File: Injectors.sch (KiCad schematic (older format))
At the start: 36 parts, among them Q1 VND14NV04, Q2 VND14NV04, Q3 VND14NV04, Q4 VND14NV04, Q5 VND14NV04, Q6 VND14NV04

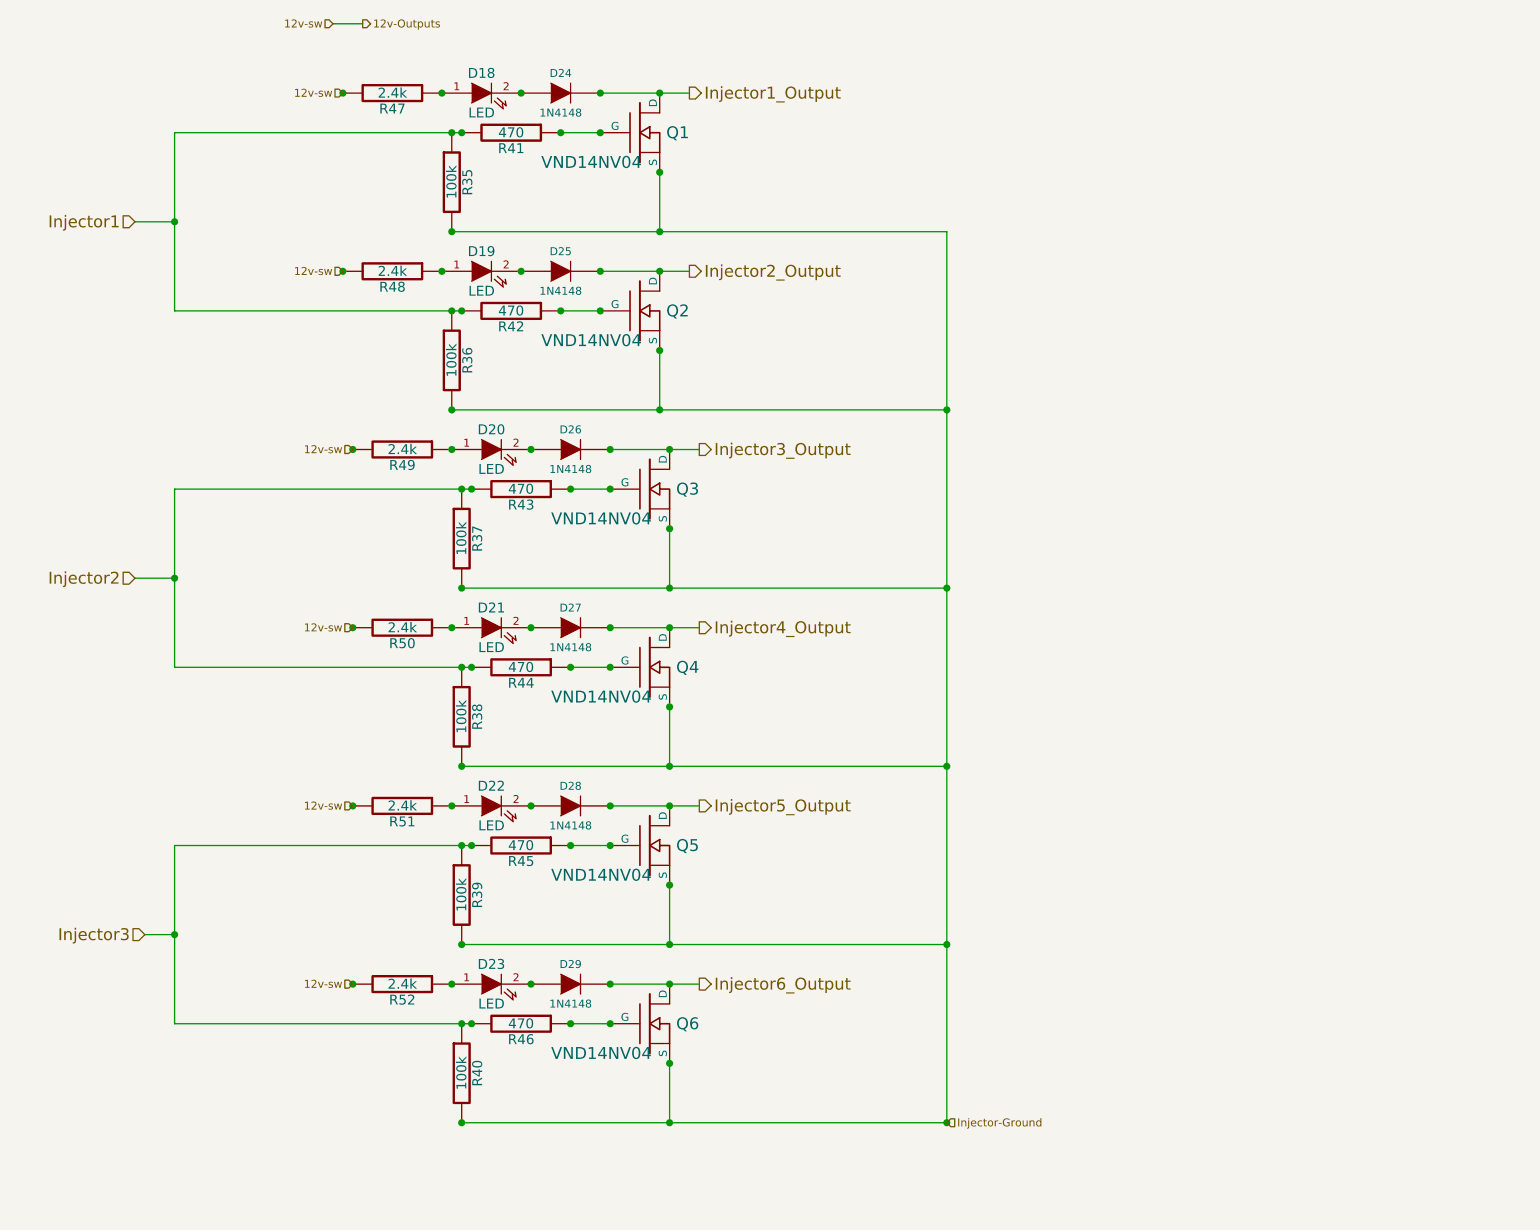
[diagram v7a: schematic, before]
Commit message: Schematics, PDF, BOM updated with latest changes
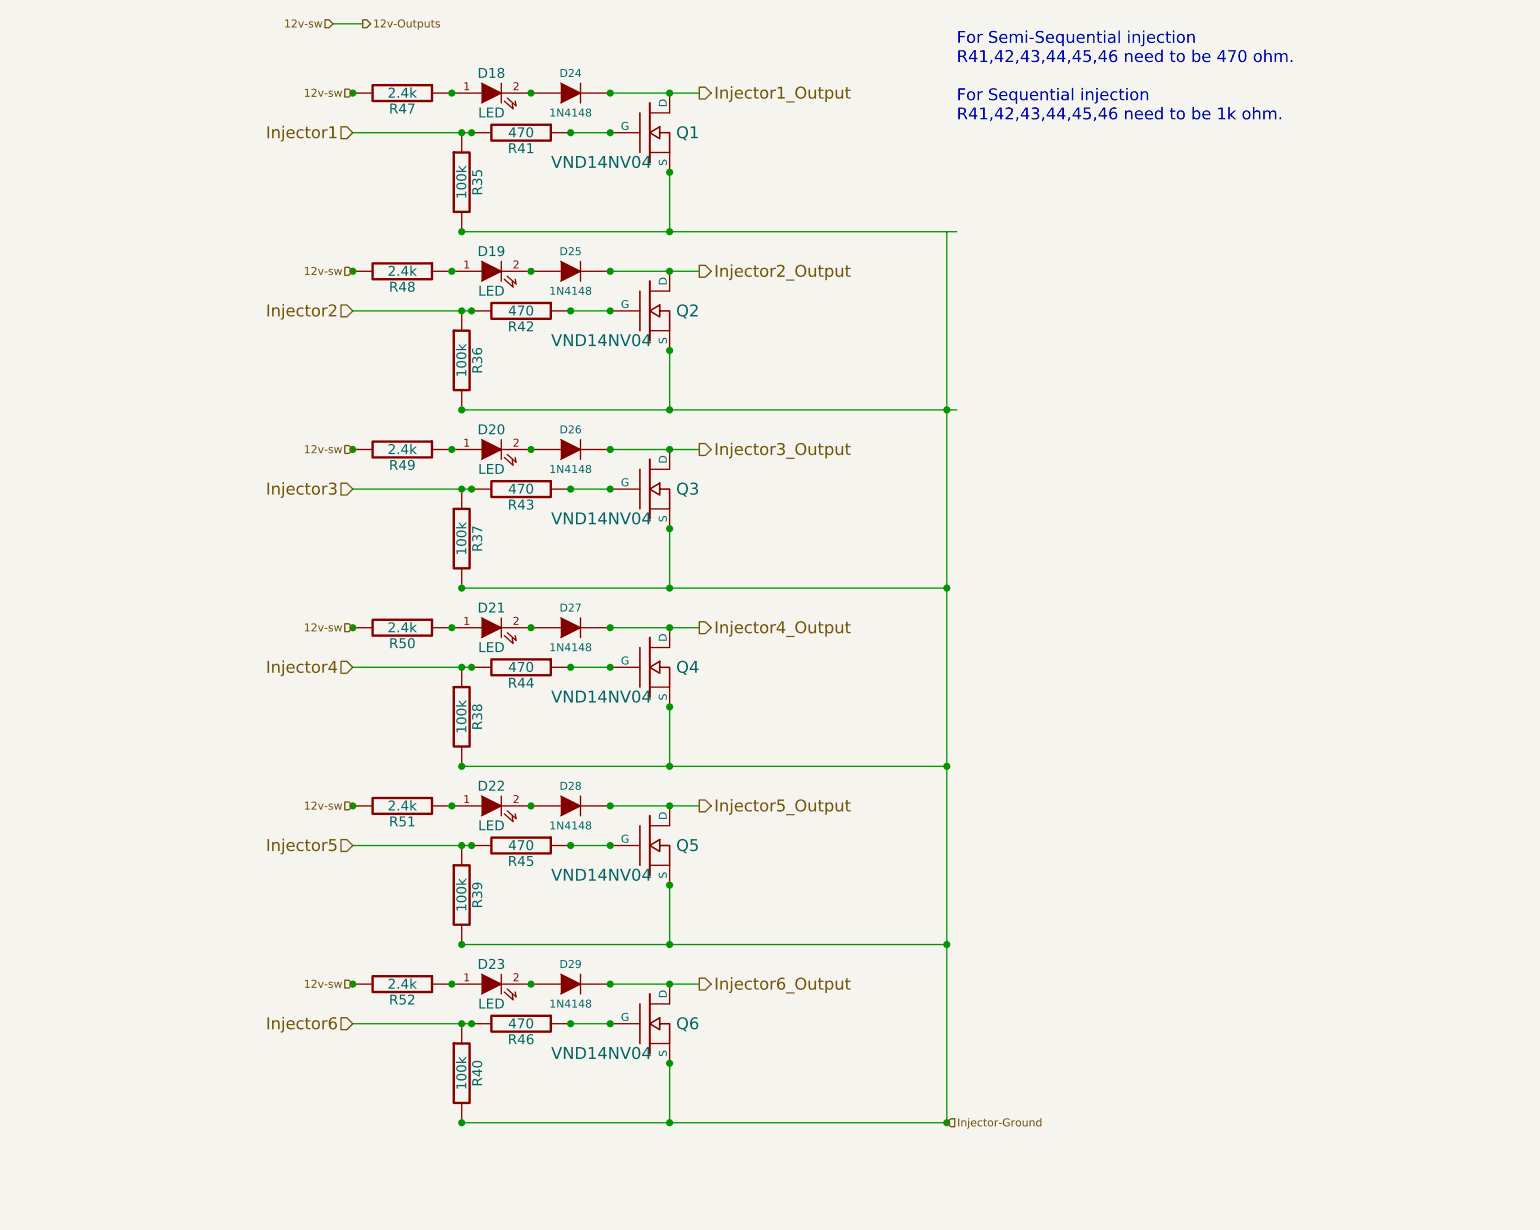
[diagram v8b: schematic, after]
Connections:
- net labels added: Injector4, Injector5, Injector6
- wire segments 38 -> 32
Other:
- note added: "For Semi-Sequential injection\nR41,42,43,44,45,46 need to be 470 ohm.\n\nFor Sequential injection \nR41,42,43,44,45,46 need to be 1k ohm."
- moved on the sheet: D18, D19, D24, D25, Q1, Q2, R35, R36, R41, R42, R47, R48
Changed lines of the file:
@@
-EESchema Schematic File Version 2  date Mon 23 Jan 2012 10:59:50 PM EST
+EESchema Schematic File Version 2  date Tue 24 Jan 2012 02:18:15 PM EST
 LIBS:power
 LIBS:device
@@
 EELAYER END
 $Descr A4 11700 8267
-Sheet 4 7
+Sheet 6 7
 Title "Jaguar PCB for FreeEMS"
 Date "24 jan 2012"
@@
 Comment4 ""
 $EndDescr
+Text Notes 5450 1400 0    60   ~ 0
+For Semi-Sequential injection\nR41,42,43,44,45,46 need to be 470 ohm.\n\nFor Sequential injection \nR41,42,43,44,45,46 need to be 1k ohm.
+Text HLabel 2400 5950 0    60   Input ~ 0
+Injector6
+Text HLabel 2400 5050 0    60   Input ~ 0
+Injector5
+Text HLabel 2400 4150 0    60   Input ~ 0
+Injector4
 Wire Wire Line
 	2300 900  2450 900
 Wire Wire Line
-	2950 2350 1500 2350
-Wire Wire Line
-	1500 2350 1500 1450
-Wire Wire Line
-	1500 1450 2950 1450
+	3000 2350 2400 2350
+Wire Wire Line
+	2400 1450 3000 1450
 Connection ~ 3700 5750
 Connection ~ 3700 4850
@@
 	3700 3050 4150 3050
 Wire Wire Line
-	3000 3250 1500 3250
-Wire Wire Line
-	1500 3250 1500 4150
-Wire Wire Line
-	1500 4150 3000 4150
-Connection ~ 3950 1950
-Wire Wire Line
-	2900 1950 5400 1950
+	3000 3250 2400 3250
+Wire Wire Line
+	2400 4150 3000 4150
+Connection ~ 4000 1950
+Wire Wire Line
+	2950 1950 5450 1950
 Connection ~ 4000 3750
 Connection ~ 5400 3750
@@
 	5400 5550 2950 5550
 Wire Wire Line
-	3000 5050 1500 5050
-Wire Wire Line
-	1500 5050 1500 5950
+	3000 5050 2400 5050
 Connection ~ 4000 6450
-Connection ~ 3950 1250
+Connection ~ 4000 1250
 Wire Wire Line
 	4000 6450 4000 6150
@@
 Connection ~ 2950 3250
 Wire Wire Line
-	3950 2850 3950 2550
-Connection ~ 2900 2850
-Wire Wire Line
-	3650 2350 3450 2350
-Connection ~ 3950 2150
-Connection ~ 3950 2550
-Connection ~ 3650 2350
-Connection ~ 3450 2350
+	4000 2850 4000 2550
+Connection ~ 2950 2850
+Wire Wire Line
+	3700 2350 3500 2350
+Connection ~ 4000 2150
+Connection ~ 4000 2550
+Connection ~ 3700 2350
+Connection ~ 3500 2350
+Connection ~ 3000 2350
 Connection ~ 2950 2350
-Connection ~ 2900 2350
-Connection ~ 2900 1450
 Connection ~ 2950 1450
-Connection ~ 3450 1450
-Connection ~ 3650 1450
-Connection ~ 3950 1650
-Wire Wire Line
-	3650 1450 3450 1450
-Connection ~ 2900 1950
-Wire Wire Line
-	3950 1950 3950 1650
-Connection ~ 3250 1250
-Connection ~ 2850 1250
-Connection ~ 2850 2150
-Connection ~ 3250 2150
+Connection ~ 3000 1450
+Connection ~ 3500 1450
+Connection ~ 3700 1450
+Connection ~ 4000 1650
+Wire Wire Line
+	3700 1450 3500 1450
+Connection ~ 2950 1950
+Wire Wire Line
+	4000 1950 4000 1650
+Connection ~ 3300 1250
+Connection ~ 2900 1250
+Connection ~ 2900 2150
+Connection ~ 3300 2150
 Connection ~ 3300 3050
 Connection ~ 2900 3050
@@
 Connection ~ 2900 5750
 Connection ~ 3300 5750
-Connection ~ 3650 1250
-Connection ~ 3650 2150
+Connection ~ 3700 1250
+Connection ~ 3700 2150
 Connection ~ 5400 6450
 Connection ~ 2400 5750
 Wire Wire Line
-	1500 5950 3000 5950
-Wire Wire Line
-	1350 5500 1500 5500
-Connection ~ 1500 5500
+	2400 5950 3000 5950
 Wire Wire Line
 	2950 6450 5400 6450
@@
 Connection ~ 4000 4650
 Wire Wire Line
-	5400 2850 2900 2850
+	5450 2850 2950 2850
 Connection ~ 5400 2850
-Connection ~ 3950 2850
+Connection ~ 4000 2850
 Connection ~ 2400 4850
 Connection ~ 2400 3950
-Wire Wire Line
-	1300 3700 1500 3700
-Connection ~ 1500 3700
 Wire Wire Line
 	3700 3950 4150 3950
@@
 Connection ~ 3700 3050
 Wire Wire Line
-	3650 1250 4100 1250
-Connection ~ 2350 1250
-Connection ~ 2350 2150
+	3700 1250 4150 1250
+Connection ~ 2400 1250
+Connection ~ 2400 2150
 Connection ~ 2400 3050
 Wire Wire Line
 	3700 5750 4150 5750
 Wire Wire Line
-	1300 1900 1500 1900
-Connection ~ 1500 1900
-Wire Wire Line
-	3650 2150 4100 2150
+	3700 2150 4150 2150
 Wire Wire Line
 	5400 6450 5400 1950
+Text HLabel 2400 1450 0    60   Input ~ 0
+Injector1
 Text HLabel 2450 900  2    40   Output ~ 0
 12v-Outputs
@@
 Text HLabel 2400 3050 0    40   Input ~ 0
 12v-sw
-Text HLabel 2350 2150 0    40   Input ~ 0
+Text HLabel 2400 2150 0    40   Input ~ 0
 12v-sw
 Text HLabel 5400 6450 2    40   Input ~ 0
 Injector-Ground
-Text HLabel 1350 5500 0    60   Input ~ 0
+Text HLabel 2400 3250 0    60   Input ~ 0
 Injector3
 $Comp
@@
 L DIODE D25
 U 1 1 4F17845F
-P 3450 2150
-F 0 "D25" H 3450 2250 40  0000 C CNN
-F 1 "1N4148" H 3450 2050 40  0000 C CNN
-	1    3450 2150
+P 3500 2150
+F 0 "D25" H 3500 2250 40  0000 C CNN
+F 1 "1N4148" H 3500 2050 40  0000 C CNN
+	1    3500 2150
 	1    0    0    -1
 $EndComp
@@
 L DIODE D24
 U 1 1 4F17842F
-P 3450 1250
-F 0 "D24" H 3450 1350 40  0000 C CNN
-F 1 "1N4148" H 3450 1150 40  0000 C CNN
-	1    3450 1250
+P 3500 1250
+F 0 "D24" H 3500 1350 40  0000 C CNN
+F 1 "1N4148" H 3500 1150 40  0000 C CNN
+	1    3500 1250
 	1    0    0    -1
 $EndComp
@@
 L LED D19
 U 1 1 4F13816D
-P 3050 2150
-F 0 "D19" H 3050 2250 50  0000 C CNN
-F 1 "LED" H 3050 2050 50  0000 C CNN
-	1    3050 2150
+P 3100 2150
+F 0 "D19" H 3100 2250 50  0000 C CNN
+F 1 "LED" H 3100 2050 50  0000 C CNN
+	1    3100 2150
 	1    0    0    -1
 $EndComp
@@
 L R R48
 U 1 1 4F13816C
-P 2600 2150
-F 0 "R48" V 2680 2150 50  0000 C CNN
-F 1 "2.4k" V 2600 2150 50  0000 C CNN
-	1    2600 2150
-	0    1    1    0
-$EndComp
-Text HLabel 2350 1250 0    40   Input ~ 0
+P 2650 2150
+F 0 "R48" V 2730 2150 50  0000 C CNN
+F 1 "2.4k" V 2650 2150 50  0000 C CNN
+	1    2650 2150
+	0    1    1    0
+$EndComp
+Text HLabel 2400 1250 0    40   Input ~ 0
 12v-sw
 $Comp
 L R R47
 U 1 1 4F1380A7
-P 2600 1250
-F 0 "R47" V 2680 1250 50  0000 C CNN
-F 1 "2.4k" V 2600 1250 50  0000 C CNN
-	1    2600 1250
+P 2650 1250
+F 0 "R47" V 2730 1250 50  0000 C CNN
+F 1 "2.4k" V 2650 1250 50  0000 C CNN
+	1    2650 1250
 	0    1    1    0
 $EndComp
@@
 L LED D18
 U 1 1 4F138097
-P 3050 1250
-F 0 "D18" H 3050 1350 50  0000 C CNN
-F 1 "LED" H 3050 1150 50  0000 C CNN
-	1    3050 1250
+P 3100 1250
+F 0 "D18" H 3100 1350 50  0000 C CNN
+F 1 "LED" H 3100 1150 50  0000 C CNN
+	1    3100 1250
 	1    0    0    -1
 $EndComp
@@
 L R R36
 U 1 1 4F0D0547
-P 2900 2600
-F 0 "R36" V 2980 2600 50  0000 C CNN
-F 1 "100k" V 2900 2600 50  0000 C CNN
-	1    2900 2600
+P 2950 2600
+F 0 "R36" V 3030 2600 50  0000 C CNN
+F 1 "100k" V 2950 2600 50  0000 C CNN
+	1    2950 2600
 	1    0    0    -1
 $EndComp
@@
 L R R42
 U 1 1 4F0D0546
-P 3200 2350
-F 0 "R42" V 3280 2350 50  0000 C CNN
-F 1 "470" V 3200 2350 50  0000 C CNN
-	1    3200 2350
+P 3250 2350
+F 0 "R42" V 3330 2350 50  0000 C CNN
+F 1 "470" V 3250 2350 50  0000 C CNN
+	1    3250 2350
 	0    1    1    0
 $EndComp
@@
 L MOSFET_N Q2
 U 1 1 4F0D0545
-P 3850 2350
-F 0 "Q2" H 4100 2350 60  0000 R CNN
-F 1 "VND14NV04" H 3860 2200 60  0000 R CNN
-	1    3850 2350
+P 3900 2350
+F 0 "Q2" H 4150 2350 60  0000 R CNN
+F 1 "VND14NV04" H 3910 2200 60  0000 R CNN
+	1    3900 2350
 	1    0    0    -1
 $EndComp
@@
 Text HLabel 4150 3050 2    60   Output ~ 0
 Injector3_Output
-Text HLabel 1300 3700 0    60   Input ~ 0
+Text HLabel 2400 2350 0    60   Input ~ 0
 Injector2
-Text HLabel 4100 2150 2    60   Output ~ 0
+Text HLabel 4150 2150 2    60   Output ~ 0
 Injector2_Output
-Text HLabel 4100 1250 2    60   Output ~ 0
+Text HLabel 4150 1250 2    60   Output ~ 0
 Injector1_Output
-Text HLabel 1300 1900 0    60   Input ~ 0
-Injector1
 $Comp
 L MOSFET_N Q1
 U 1 1 4F062E00
-P 3850 1450
-F 0 "Q1" H 4100 1450 60  0000 R CNN
-F 1 "VND14NV04" H 3860 1300 60  0000 R CNN
-	1    3850 1450
+P 3900 1450
+F 0 "Q1" H 4150 1450 60  0000 R CNN
+F 1 "VND14NV04" H 3910 1300 60  0000 R CNN
+	1    3900 1450
 	1    0    0    -1
 $EndComp
@@
 L R R41
 U 1 1 4F062C55
-P 3200 1450
-F 0 "R41" V 3280 1450 50  0000 C CNN
-F 1 "470" V 3200 1450 50  0000 C CNN
-	1    3200 1450
+P 3250 1450
+F 0 "R41" V 3330 1450 50  0000 C CNN
+F 1 "470" V 3250 1450 50  0000 C CNN
+	1    3250 1450
 	0    1    1    0
 $EndComp
@@
 L R R35
 U 1 1 4F062C4D
-P 2900 1700
-F 0 "R35" V 2980 1700 50  0000 C CNN
-F 1 "100k" V 2900 1700 50  0000 C CNN
-	1    2900 1700
-	1    0    0    -1
-$EndComp
+P 2950 1700
+F 0 "R35" V 3030 1700 50  0000 C CNN
+F 1 "100k" V 2950 1700 50  0000 C CNN
+	1    2950 1700
+	1    0    0    -1
+$EndComp
